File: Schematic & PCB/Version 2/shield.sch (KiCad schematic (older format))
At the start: 21 parts, among them J1 CONN_POWER, J2 CONN_POWER_H, P1 CONN_SENSOR_SERIAL, P2 CONN_SENSOR_SERIAL_H, P3 CONN_PROG, Q1 ZVN4206A, U1 SN74LVC245A, U2 ESP-01v090, U3 ESP-12, U4 LD1117S33CTR

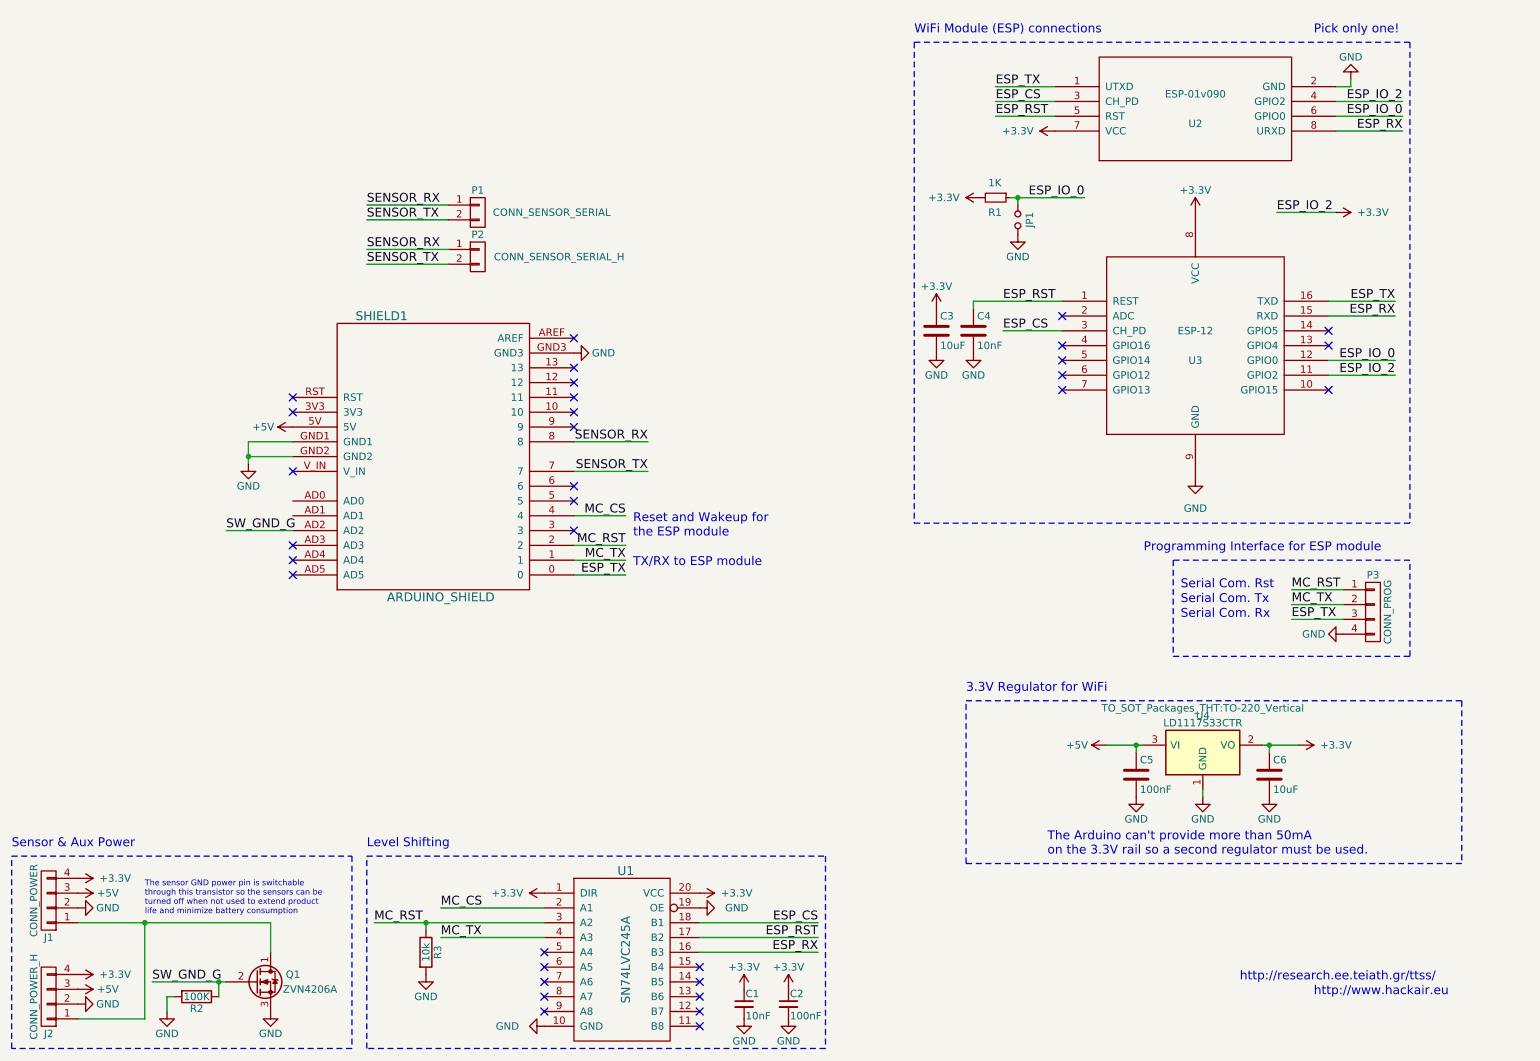
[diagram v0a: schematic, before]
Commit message: Shield design revision (v2.2)
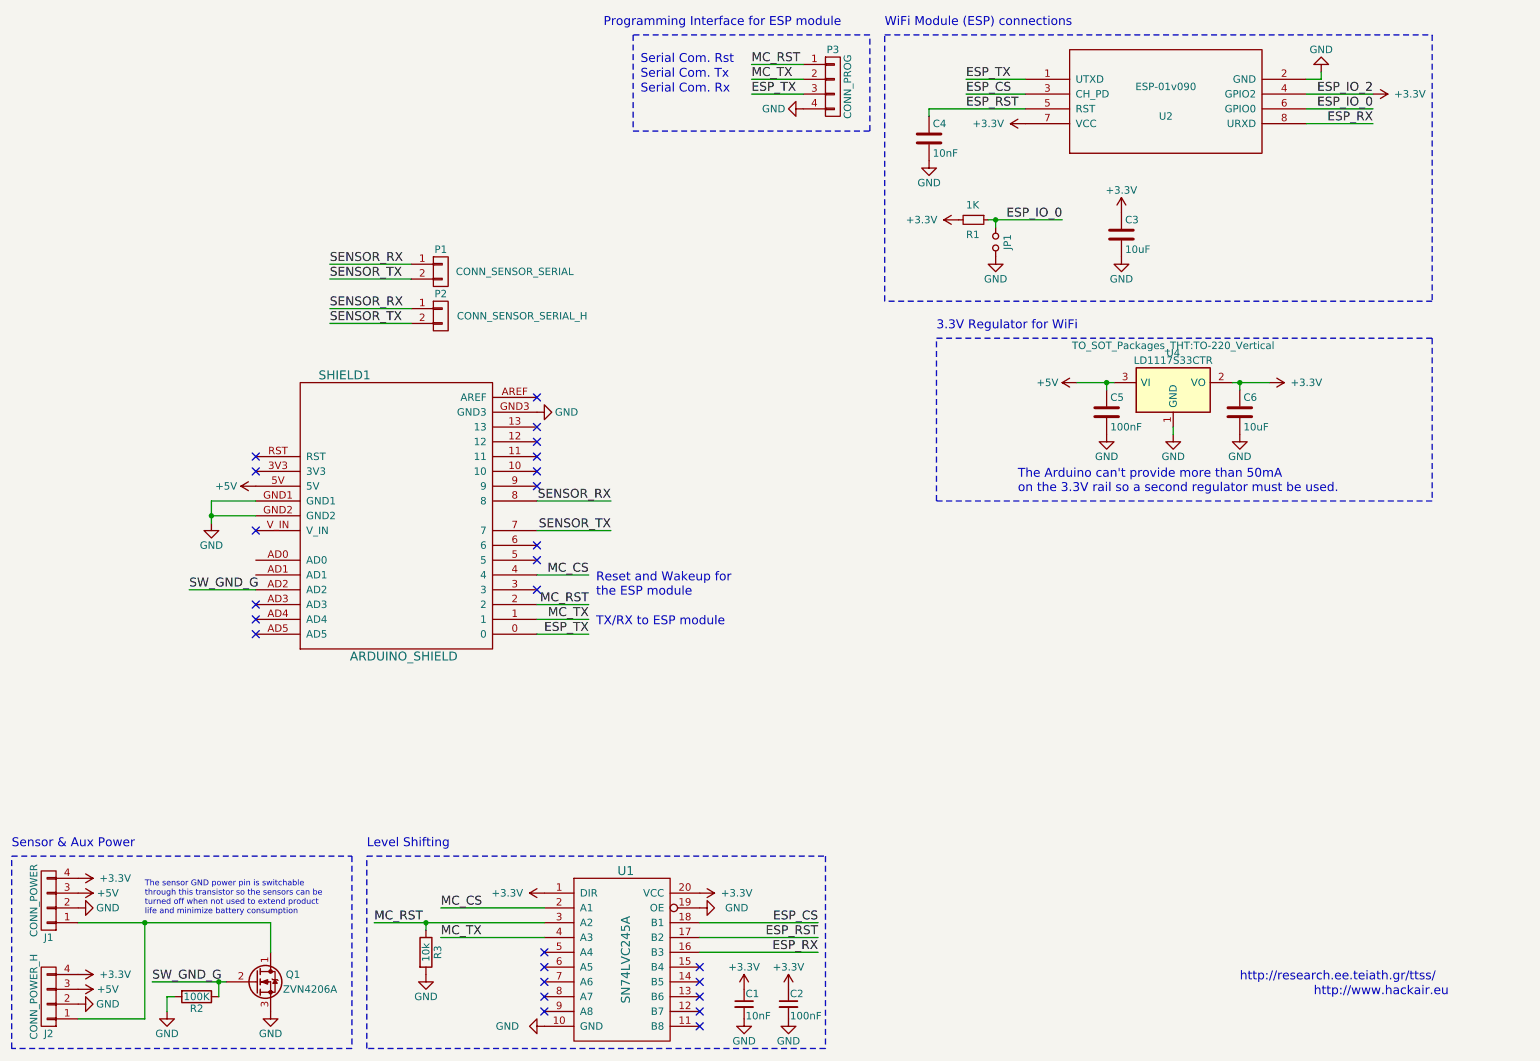
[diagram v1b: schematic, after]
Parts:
- removed U3: ESP-12, ESP8266:ESP-12, symbol ESP-12
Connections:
- no-connect marks 33 -> 25
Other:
- note removed: "Pick only one!"
- moved on the sheet: C3, C4, C5, C6, JP1, P1, P2, P3, R1, SHIELD1, U2, U4
